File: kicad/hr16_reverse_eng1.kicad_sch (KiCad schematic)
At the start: 0 parts

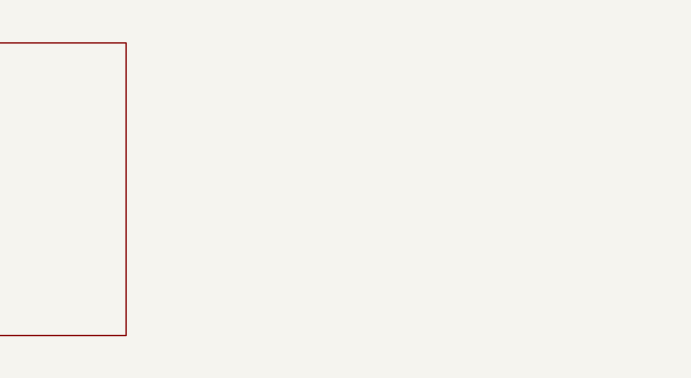
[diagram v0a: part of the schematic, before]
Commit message: Added LCD replacement schematic (untested)
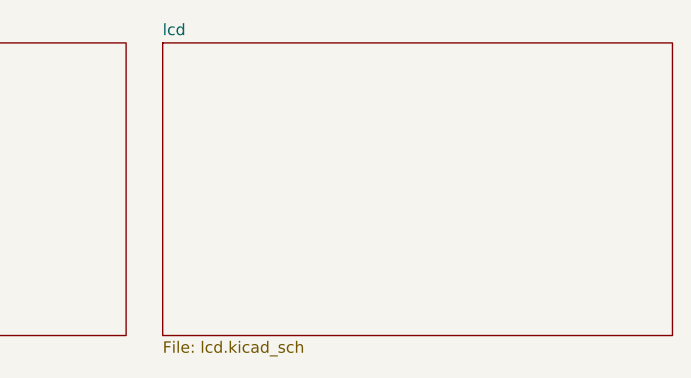
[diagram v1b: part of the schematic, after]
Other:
- added sheet lcd (lcd.kicad_sch)
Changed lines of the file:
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@@
+		)
+	)
+	(sheet
+		(at 195.834 27.178)
+		(size 56.642 32.512)
+		(fields_autoplaced yes)
+		(stroke
+			(width 0.1524)
+			(type solid)
+		)
+		(fill
+			(color 0 0 0 0.0000)
+		)
+		(property "Sheetname" "lcd"
+			(at 195.834 26.4664 0)
+			(effects
+				(font
+					(size 1.27 1.27)
+				)
+				(justify left bottom)
+			)
+		)
+		(property "Sheetfile" "lcd.kicad_sch"
+			(at 195.834 60.2746 0)
+			(effects
+				(font
+					(size 1.27 1.27)
+				)
+				(justify left top)
+			)
+		)
+		(instances
+			(project "hr16_reverse_eng1"
+				(path "/99eda9a6-00e0-493c-b2d1-8a5acb1e41f8"
+					(page "5")
+				)
+			)
 		)
 	)
